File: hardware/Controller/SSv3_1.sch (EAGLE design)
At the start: 197 parts, among them Q1 20.000_MHZ, Q2 200mA/50V, X1 PN61729-S, X2 SCAN_LED, X3 RJ45-6L-B, X4 C-GRID-06-74099

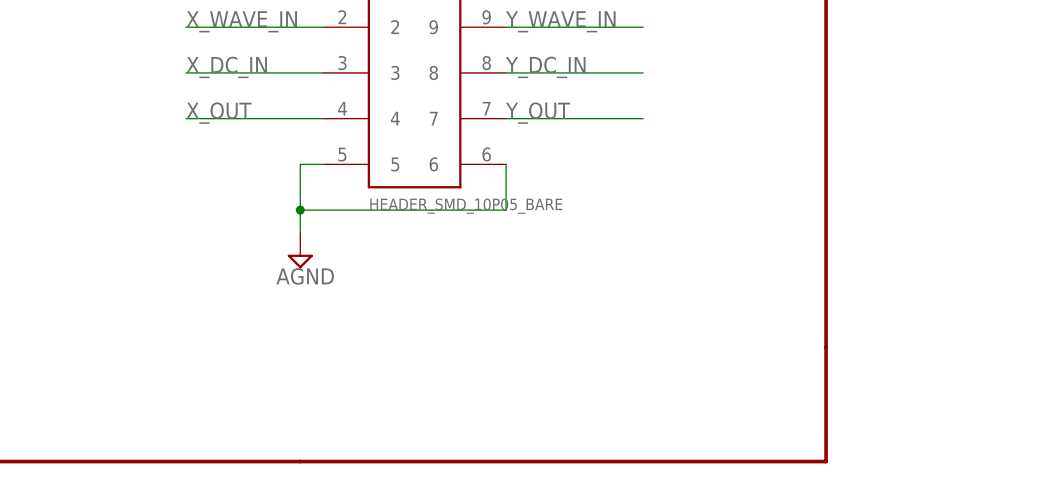
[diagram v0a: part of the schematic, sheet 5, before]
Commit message: Finished adding license to files.  Added .pdf of the hardware.  Added .zip with current software build.
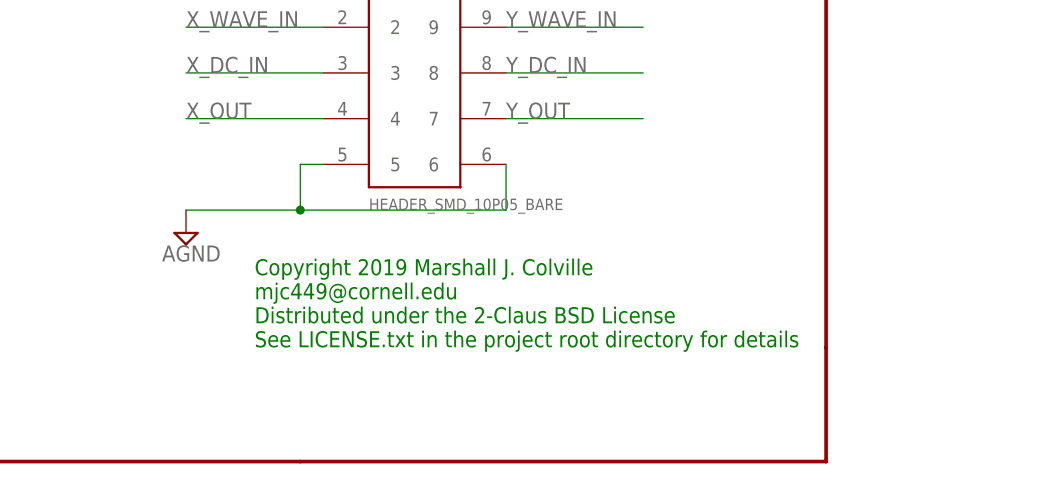
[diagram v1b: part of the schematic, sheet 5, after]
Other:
- note added: "Copyright 2019 Marshall J. Colville mjc449@cornell.edu Distributed under the 2-Claus BSD License See LICENSE.txt in the project root directory for details"
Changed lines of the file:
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@@
 RD0..9 DATA
 RD10..11 ADDRESS</text>
+<text x="187.96" y="12.7" size="1.778" layer="91">Copyright 2019 Marshall J. Colville
+mjc449@cornell.edu
+Distributed under the 2-Claus BSD License
+See LICENSE.txt in the project root directory for details</text>
 </plain>
 <instances>
@@
 <description>DIO, POWER, MISC</description>
 <plain>
+<text x="185.42" y="12.7" size="1.778" layer="91">Copyright 2019 Marshall J. Colville
+mjc449@cornell.edu
+Distributed under the 2-Claus BSD License
+See LICENSE.txt in the project root directory for details</text>
 </plain>
 <instances>
@@
 <text x="172.72" y="129.54" size="1.778" layer="91">For use with OEM MD SnC Driver:
 Connect +24 V supply</text>
+<text x="185.42" y="12.7" size="1.778" layer="91">Copyright 2019 Marshall J. Colville
+mjc449@cornell.edu
+Distributed under the 2-Claus BSD License
+See LICENSE.txt in the project root directory for details</text>
 </plain>
 <instances>
@@
 <description>AUX_DAC</description>
 <plain>
+<text x="185.42" y="12.7" size="1.778" layer="91">Copyright 2019 Marshall J. Colville
+mjc449@cornell.edu
+Distributed under the 2-Claus BSD License
+See LICENSE.txt in the project root directory for details</text>
 </plain>
 <instances>
@@
 SMD PASSIVES: 0603 IMPERIAL
 SMD RESISTORS: 1% OR BETTER</text>
+<text x="185.42" y="12.7" size="1.778" layer="91">Copyright 2019 Marshall J. Colville
+mjc449@cornell.edu
+Distributed under the 2-Claus BSD License
+See LICENSE.txt in the project root directory for details</text>
 </plain>
 <instances>
@@
 <instance part="U$1" gate="G$1" x="203.2" y="43.18"/>
 <instance part="SUPPLY63" gate="G$1" x="48.26" y="78.74"/>
-<instance part="SUPPLY65" gate="G$1" x="190.5" y="22.86"/>
+<instance part="SUPPLY65" gate="G$1" x="177.8" y="25.4"/>
 </instances>
 <busses>
@@
 <wire x1="190.5" y1="27.94" x2="190.5" y2="33.02" width="0.1524" layer="91"/>
 <pinref part="SUPPLY65" gate="G$1" pin="AGND"/>
-<wire x1="190.5" y1="27.94" x2="190.5" y2="25.4" width="0.1524" layer="91"/>
+<wire x1="190.5" y1="27.94" x2="177.8" y2="27.94" width="0.1524" layer="91"/>
 <junction x="190.5" y="27.94"/>
 </segment>
@@
 <plain>
 <text x="127" y="175.26" size="1.778" layer="91">C56, C61 OPTIONAL COMPENSATING CAPS, APPLY IF NECESSARY FOR STABILITY</text>
+<text x="185.42" y="12.7" size="1.778" layer="91">Copyright 2019 Marshall J. Colville
+mjc449@cornell.edu
+Distributed under the 2-Claus BSD License
+See LICENSE.txt in the project root directory for details</text>
 </plain>
 <instances>
